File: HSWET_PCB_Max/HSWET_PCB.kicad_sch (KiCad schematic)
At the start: 21 parts, among them IC3 PS2565L-1-V-F3-A, IC4 PS2565L-1-V-F3-A, IC5 PS2565L-1-V-F3-A, J1 CON-SOCJ-2155, J2 Conn_01x05, J3 CON-SOCJ-2155, U1 INA260AIPWR, U2 YAAJ_DCDC_StepDown_LM2596, U3 YAAJ_DCDC_StepDown_LM2596

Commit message: x
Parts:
- U1: footprint wsg_fp:SOP65P490X110-8N -> footprints.:ina260
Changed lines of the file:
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@@
 	(global_label "Turbine_PWR_Sensed"
 		(shape output)
-		(at 152.4 48.26 180)
+		(at 153.67 48.26 180)
 		(fields_autoplaced yes)
 		(effects
@@
 		)
 		(property "Intersheetrefs" "${INTERSHEET_REFS}"
-			(at 129.8812 48.26 0)
+			(at 131.1512 48.26 0)
 			(effects
 				(font
@@
 			)
 		)
-		(property "Footprint" "wsg_fp:SOP65P490X110-8N"
+		(property "Footprint" "footprints.:ina260"
 			(at 171.45 50.8 0)
 			(effects

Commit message: routing done
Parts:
- A1: footprint Module:Arduino_UNO_R3 -> footprints.:ARDUINO_ARDUINO_UNO_REV3
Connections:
- net Turbine_PWR: no longer D2.1 (A1), IC5.1 (ANODE_CATHODE), S1.3, U1.14 (IN-), U1.15 (IN-), U1.16 (IN-)
- new net Turbine_PWR_Sensed: D2.1 (A1), IC5.1 (ANODE_CATHODE), S1.3, U1.14 (IN-), U1.15 (IN-), U1.16 (IN-)
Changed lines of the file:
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@@
 		(exclude_from_sim no)
 		(at 13.97 20.32 0)
-		(size 99.06 66.04)
+		(size -99.06 66.04)
 		(margins 0.9525 0.9525 0.9525 0.9525)
 		(stroke
@@
 				(size 1.27 1.27)
 			)
-			(justify left top)
+			(justify right top)
 		)
 	)
@@
 	)
 	(junction
-		(at 153.67 45.72)
-		(diameter 0)
-		(color 0 0 0 0)
-	)
-	(junction
 		(at 195.58 35.56)
 		(diameter 0)
@@
 	)
 	(junction
-		(at 153.67 48.26)
-		(diameter 0)
-		(color 0 0 0 0)
-	)
-	(junction
 		(at 106.68 107.95)
 		(diameter 0)
@@
 	(wire
 		(pts
-			(xy 153.67 45.72) (xy 153.67 48.26)
-		)
-		(stroke
-			(width 0)
-			(type default)
-		)
-	)
-	(wire
-		(pts
 			(xy 134.62 58.42) (xy 134.62 62.23)
 		)
@@
 	(global_label "Turbine_PWR_Sensed"
 		(shape output)
-		(at 153.67 48.26 180)
+		(at 152.4 48.26 180)
 		(fields_autoplaced yes)
 		(effects
@@
 		)
 		(property "Intersheetrefs" "${INTERSHEET_REFS}"
-			(at 131.1512 48.26 0)
+			(at 129.8812 48.26 0)
 			(effects
 				(font
@@
 			)
 		)
-		(property "Footprint" "Module:Arduino_UNO_R3"
+		(property "Footprint" "footprints.:ARDUINO_ARDUINO_UNO_REV3"
 			(at 167.64 114.3 0)
 			(effects
@@
 			)
 		)
-		(property "Footprint" "Module:Arduino_UNO_R3"
+		(property "Footprint" "footprints.:ARDUINO_ARDUINO_UNO_REV3"
 			(at 210.82 113.03 0)
 			(effects
@@
 			)
 		)
-		(property "Footprint" "Module:Arduino_UNO_R3"
+		(property "Footprint" "footprints.:ARDUINO_ARDUINO_UNO_REV3"
 			(at 215.9 148.59 0)
 			(effects
@@
 			)
 		)
-		(property "Footprint" "Module:Arduino_UNO_R3"
+		(property "Footprint" "footprints.:ARDUINO_ARDUINO_UNO_REV3"
 			(at 170.18 148.59 0)
 			(effects

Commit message: Integrated safety
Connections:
- net 5V: no longer U3.4 (Vout)
- net Safety Signal: now reaches A1.D4
- new net 5V_BUCK: U3.4 (Vout)
- no-connect marks 27 -> 26
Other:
- added sheet Safety System (Safety System.kicad_sch)
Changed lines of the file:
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@@
 	(text_box "5V_AND_6V_BUCK/BOOST_CONVERTER"
 		(exclude_from_sim no)
-		(at 13.97 20.32 0)
-		(size -99.06 66.04)
+		(at 15.24 21.59 0)
+		(size 99.06 66.04)
 		(margins 0.9525 0.9525 0.9525 0.9525)
 		(stroke
@@
 	)
 	(no_connect
-		(at 223.52 110.49)
-	)
-	(no_connect
 		(at 154.94 106.68)
 	)
@@
 		)
 	)
-	(global_label "Turbine_PWR_Sensed"
-		(shape input)
-		(at 30.48 62.23 0)
-		(fields_autoplaced yes)
-		(effects
-			(font
-				(size 1.27 1.27)
-			)
-			(justify left)
-		)
-		(property "Intersheetrefs" "${INTERSHEET_REFS}"
-			(at 52.9988 62.23 0)
-			(effects
-				(font
-					(size 1.27 1.27)
-				)
-				(justify left)
-				(hide yes)
-			)
-		)
-	)
 	(global_label "9V"
 		(shape output)
@@
 		)
 	)
-	(global_label "5V"
+	(global_label "5V_BUCK"
 		(shape output)
 		(at 86.36 58.42 0)
@@
 		)
 		(property "Intersheetrefs" "${INTERSHEET_REFS}"
-			(at 91.6433 58.42 0)
+			(at 97.7514 58.42 0)
 			(effects
 				(font
@@
 		)
 	)
+	(global_label "Safety Signal"
+		(shape input)
+		(at 223.52 110.49 0)
+		(fields_autoplaced yes)
+		(effects
+			(font
+				(size 1.27 1.27)
+			)
+			(justify left)
+		)
+		(property "Intersheetrefs" "${INTERSHEET_REFS}"
+			(at 239.2654 110.49 0)
+			(effects
+				(font
+					(size 1.27 1.27)
+				)
+				(justify left)
+				(hide yes)
+			)
+		)
+	)
 	(global_label "5V"
 		(shape input)
@@
 				)
 			)
+		)
+	)
+	(sheet
+		(at 264.16 123.19)
+		(size 12.7 3.81)
+		(exclude_from_sim no)
+		(in_bom yes)
+		(on_board yes)
+		(dnp no)
+		(fields_autoplaced yes)
+		(stroke
+			(width 0.1524)
+			(type solid)
+		)
+		(fill
+			(color 0 0 0 0.0000)
+		)
+		(property "Sheetname" "Safety System"
+			(at 264.16 122.4784 0)
+			(effects
+				(font
+					(size 1.27 1.27)
+				)
+				(justify left bottom)
+			)
+		)
+		(property "Sheetfile" "Safety System.kicad_sch"
+			(at 264.16 127.5846 0)
+			(effects
+				(font
+					(size 1.27 1.27)
+				)
+				(justify left top)
+			)
+		)
+		(instances
+			(project "HSWET_PCB"
+				(path "/82d46295-621f-4df3-b604-ae215ede48d5"
+					(page "2")
+				)
+			)

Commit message: Completed layout for safety system
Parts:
- U1: footprint footprints.:ina260 -> footprints:ina260
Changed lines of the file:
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@@
 			)
 		)
-		(property "Footprint" "footprints.:ina260"
+		(property "Footprint" "footprints:ina260"
 			(at 171.45 50.8 0)
 			(effects

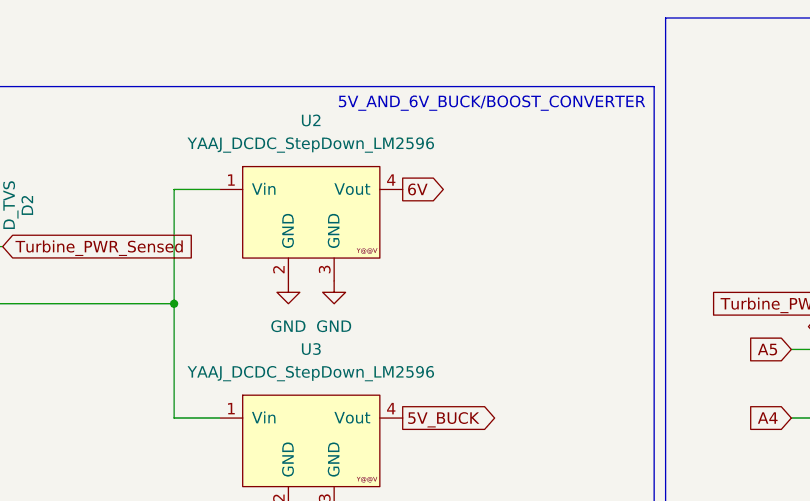
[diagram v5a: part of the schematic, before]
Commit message: swithced resistor and diode
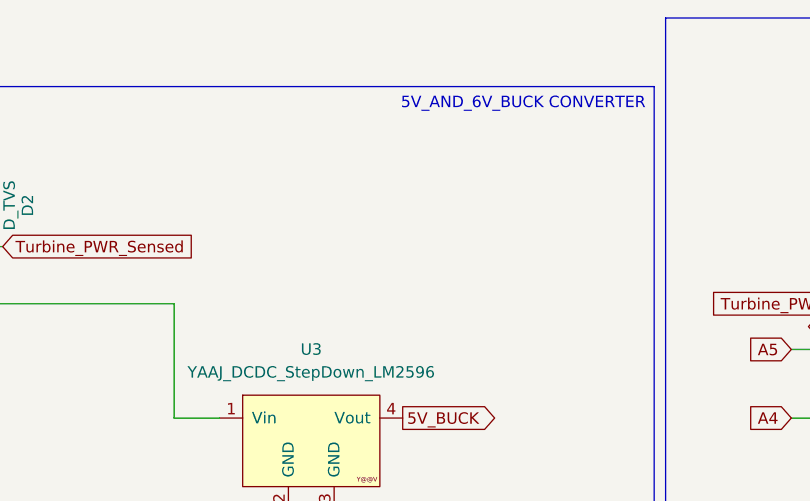
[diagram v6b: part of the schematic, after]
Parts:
- removed U2: YAAJ_DCDC_StepDown_LM2596, footprints:TO263-5, symbol LM2596:YAAJ_DCDC_StepDown_LM2596

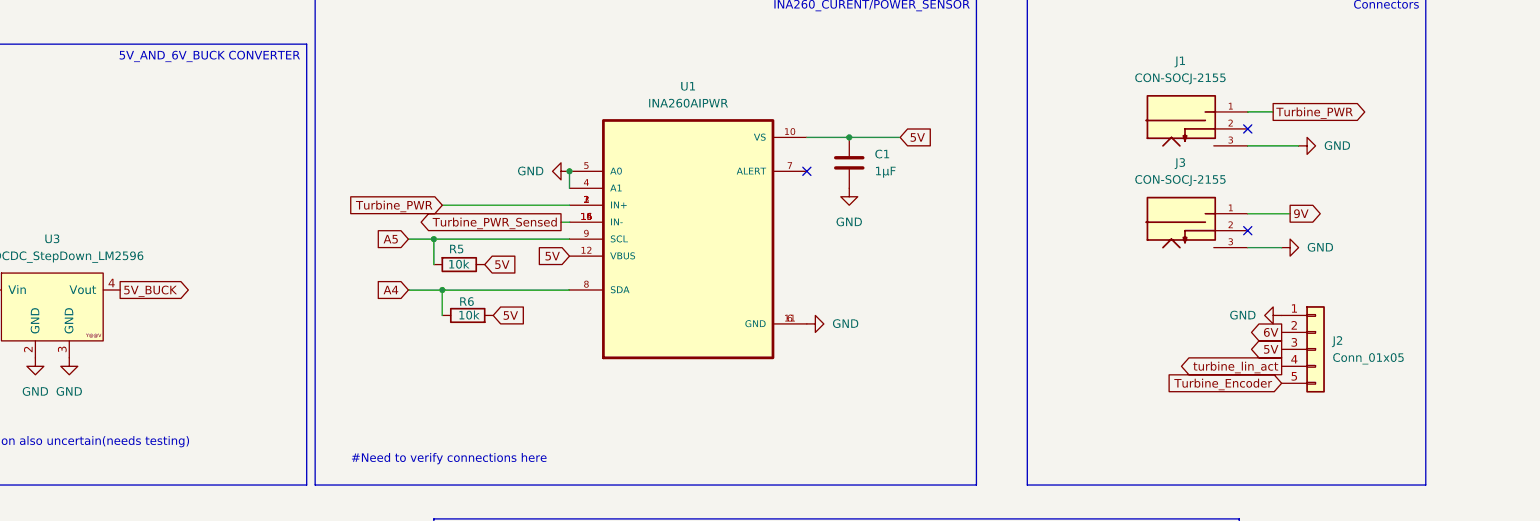
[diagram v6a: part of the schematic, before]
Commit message: added maybe unecessary plane, swapped 1x05 connector -> 1x04 after mirabel got rid of 6v, ficed footprint for lm2596
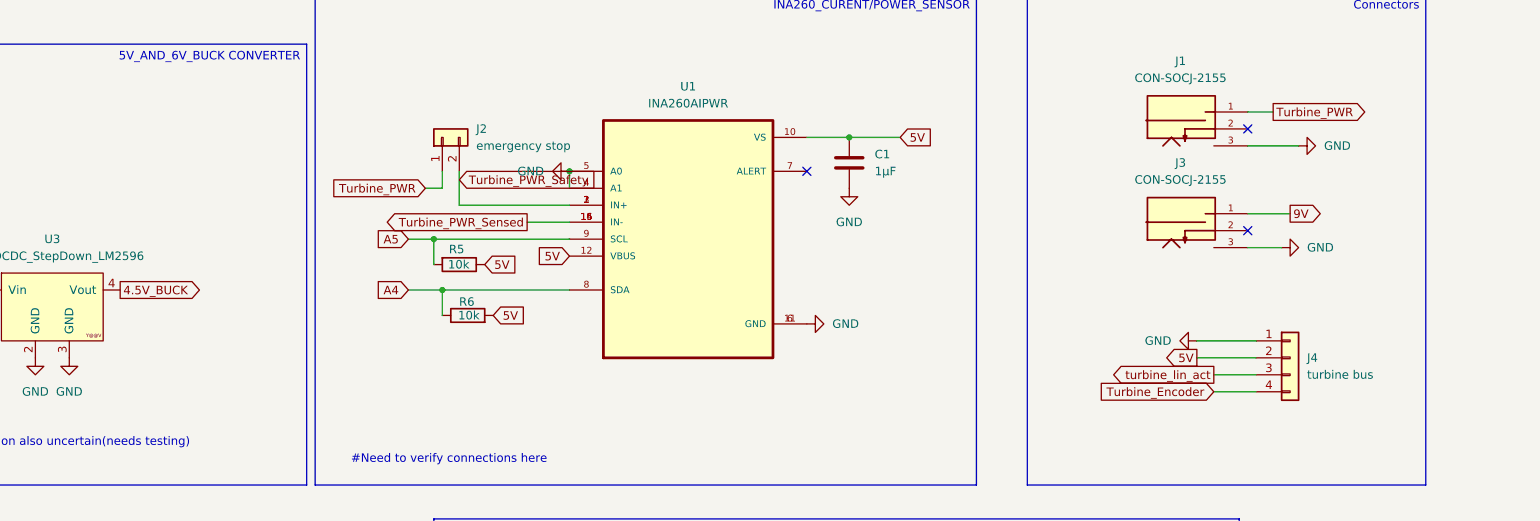
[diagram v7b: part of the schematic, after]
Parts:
- removed J2: Conn_01x05, Connector_PinHeader_1.27mm:PinHeader_1x05_P1.27mm_Horizontal, symbol Connector_Generic:Conn_01x05
- added J2: emergency stop, Connector_PinHeader_2.54mm:PinHeader_1x02_P2.54mm_Vertical, symbol Connector_Generic:Conn_01x02
- added J4: turbine bus, Connector_PinHeader_2.54mm:PinHeader_1x04_P2.54mm_Horizontal, symbol Connector_Generic:Conn_01x04
- U3: footprint footprints:TO263-5 -> footprints:YAAJ_DCDC_StepDown_LM2596
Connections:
- net 5V: now also J4.2 (Pin_2)
- net GND: now also J4.1 (Pin_1)
- net Turbine_Encoder: now also J4.4 (Pin_4)
- net Turbine_PWR: now also J2.1 (Pin_1); no longer U1.1 (IN+), U1.2 (IN+), U1.3 (IN+)
- net turbine_lin_act: now also J4.3 (Pin_3)
- net 5V_BUCK renamed 4.5V_BUCK
- new net Turbine_PWR_Safety: J2.2 (Pin_2), U1.1 (IN+), U1.2 (IN+), U1.3 (IN+)

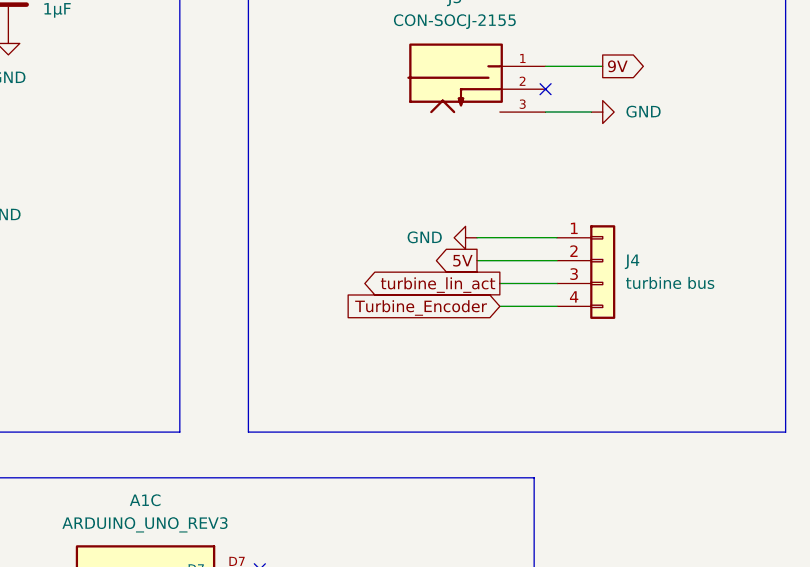
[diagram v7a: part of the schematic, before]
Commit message: new routing for pcb, some smaller ports still unrouted
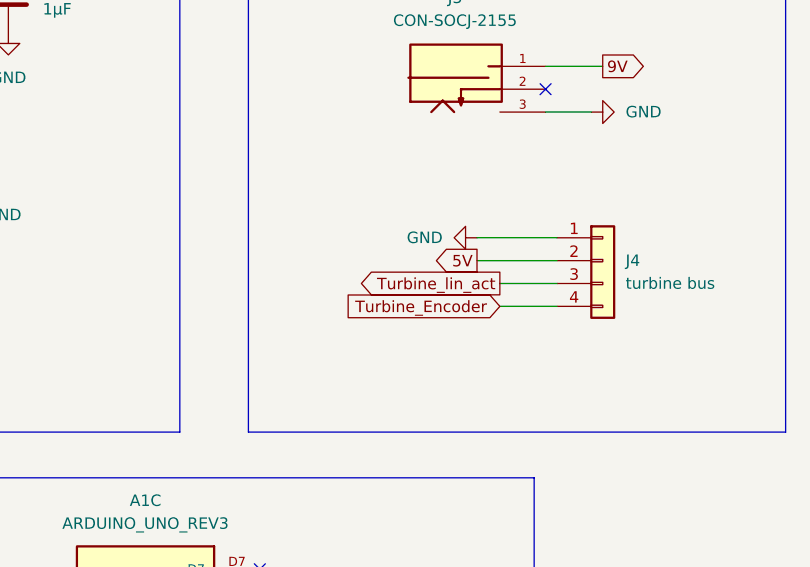
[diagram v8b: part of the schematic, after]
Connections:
- net turbine_lin_act is gone; now on net Turbine_lin_act: J4.3 (Pin_3)
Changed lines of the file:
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@@
 		)
 	)
-	(global_label "turbine_lin_act"
+	(global_label "Turbine_lin_act"
 		(shape output)
 		(at 250.19 71.12 180)
@@
 		)
 		(property "Intersheetrefs" "${INTERSHEET_REFS}"
-			(at 233.235 71.12 0)
+			(at 232.9931 71.12 0)
 			(effects
 				(font
